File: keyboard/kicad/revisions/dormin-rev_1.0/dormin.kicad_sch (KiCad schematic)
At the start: 59 parts, among them J2 Conn_01x07_Socket, SW1 SW_Push, SW10 SW_Push, SW11 SW_Push, SW12 SW_Push, SW13 SW_Push, SW14 SW_Push, SW15 SW_Push, SW16 SW_Push, SW17 SW_Push, SW18 SW_Push, SW19 SW_Push, SW2 SW_Push, SW20 SW_Push, SW3 SW_Push, SW4 SW_Push, SW5 SW_Push, SW6 SW_Push, SW7 SW_Push, SW8 SW_Push, SW9 SW_Push, U2 ER_OLEDM0.91_1x-I2C, U3 XIAO-nRF52840-Plus-SMD

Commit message: feat: update schematics
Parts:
- added D27: D_Schottky, symbol Device:D_Schottky
- added D28: SMF5V0A, Diode_SMD:D_SMF, symbol Diode:SMF5V0A
- added F2: Polyfuse, symbol Device:Polyfuse
- added J3: Pogo Connector, symbol Connector:Conn_01x04_Pin
- added R5, R6: 33R, symbol Device:R
- added U4: TPD2E2U06DCK, Package_TO_SOT_SMD:SOT-323_SC-70, symbol Power_Protection:TPD2E2U06DCK
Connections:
- net BAT- is gone; now on net GND: U3.29 (GND)
- net +3V3: no longer D21.3 (VDD), D22.3 (VDD), D23.3 (VDD), D24.3 (VDD), J2.4 (Pin_4), U3.12 (3V3_OUT)
- net D18: no longer U3.22 (D18_MISO)
- net D8: no longer U3.9 (D8_SCK)
- net D9: no longer U3.10 (D9_MISO)
- net GND: now also JST1.1 (Pin_1), D28.1 (A1), J3.1 (Pin_1), U4.3; no longer JST1.2 (Pin_2)
- net MOSI: no longer U3.23 (D19_MOSI)
- net SCK: no longer U3.21 (D17_SCK)
- net at BT1.1 (+), PSW1.3 (C): now also JST1.2 (Pin_2); no longer JST1.1 (Pin_1)
- net USB_VBUS: now reaches U3.14 (VBUS)
- net USB_VBUS: now also F2.1
- net LED renamed COL4
- net COL4: now also SW13.2, SW19.2, SW2.2, SW7.2; no longer D21.2 (DIN)
- net col0 renamed COL0
- net col1 renamed COL1
- net COL1: now also U3.8 (D7_RX); no longer U3.15 (D11_SD)
- net col2 renamed COL2
- net COL2: now also U3.9 (D8_SCK); no longer U3.16 (D12_SCK)
- net col3 renamed COL3
- net COL3: now also U3.10 (D9_MISO); no longer U3.17 (D13_WS)
- removed net col4: SW13.2, SW19.2, SW2.2, SW7.2, U3.18 (D14_NFC1)
- net col5 renamed COL5
- net COL5: now also U3.15 (D11_SD); no longer U3.8 (D7_RX)
- net row0 renamed ROW0
- net row1 renamed ROW1
- net row2 renamed ROW2
- net row3 renamed ROW3
- new net: J3.3 (Pin_3), R5.1, U4.1
- new net: D27.1 (K), D28.2 (A2), J3.2 (Pin_2)
- new net: J3.4 (Pin_4), R6.2, U4.2
- new net: D27.2 (A), F2.2
- new net EXT_D17: R6.1, U3.21 (D17_SCK)
- new net EXT_D19: R5.2, U3.23 (D19_MOSI)
- new net RGB_DATA: D21.2 (DIN), U3.17 (D13_WS)
- new net VCC: D21.3 (VDD), D22.3 (VDD), D23.3 (VDD), D24.3 (VDD), J2.4 (Pin_4), U3.12 (3V3_OUT)
- no-connect marks 3 -> 5
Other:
- note added: "Pogo Extension"
- moved on the sheet: BT1, JST1, MH1, MH2, MH3, MH4, PSW1, TP1, TP2, U3

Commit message: feat: clean pcb and outline
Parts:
- removed D25: 1N4148W, Diode_SMD:D_SOD-123, symbol Diode:1N4148W
- removed RES1: RotaryEncoder_Switch, willkeebs_peripherals:RotaryEncoder_Alps_EC11E-Switch_Vertical_H20mm-keebio_modified, symbol Device:RotaryEncoder_Switch
- removed U2: ER_OLEDM0.91_1x-I2C, Display:ER_OLEDM0.91_1x-I2C, symbol Display_Graphic:ER_OLEDM0.91_1x-I2C
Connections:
- net D18 is gone; now on net EXTD: J2.7 (Pin_7)
- net D8 is gone; now on net EXTA: J2.1 (Pin_1)
- net D9 is gone; now on net EXTB: J2.6 (Pin_6)
- net MOSI is gone; now on net GND: J2.2 (Pin_2)
- net SCK is gone; now on net VCC: J2.3 (Pin_3)
- net GND: no longer J2.5 (Pin_5)
- net SCL: now also J2.4 (Pin_4)
- net SDA: now also J2.5 (Pin_5)
- net VCC: no longer J2.4 (Pin_4)
- net EXTA: now reaches U3.16 (D12_SCK)
- net EXTB: now reaches U3.18 (D14_NFC1)
- net EXTD: now reaches U3.22 (D18_MISO)
- net ENCA renamed EXTG
- net ENCB renamed EXTF
- net EXT_D17 renamed EXTE
- net EXT_D19 renamed EXTC
- no-connect marks 5 -> 2
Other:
- note removed: "OLED SSD1306"
- moved on the sheet: BT1, J2, JST1, PSW1, TP1, TP2, U3

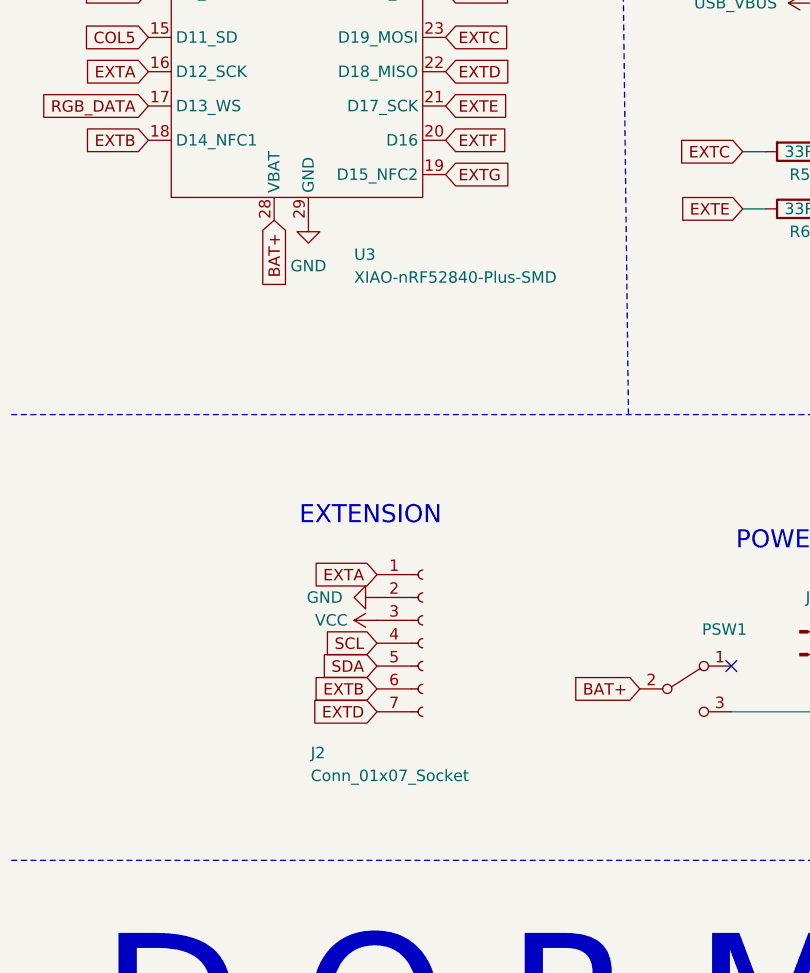
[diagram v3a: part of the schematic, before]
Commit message: feat: start PCB placement
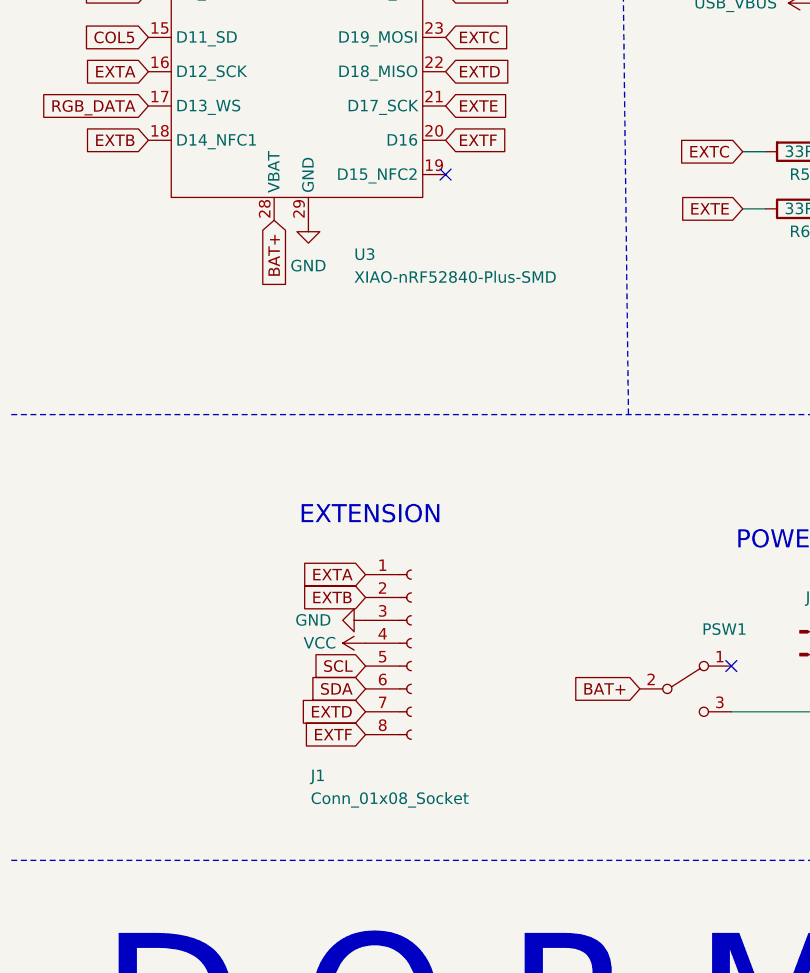
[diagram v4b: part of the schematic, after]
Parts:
- removed J2: Conn_01x07_Socket, symbol Connector:Conn_01x07_Socket
- added J1: Conn_01x08_Socket, Connector_PinSocket_2.54mm:PinSocket_1x08_P2.54mm_Vertical, symbol Connector:Conn_01x08_Socket
- J3: footprint (none) -> Connector_PinSocket_2.54mm:PinSocket_1x04_P2.54mm_Vertical_SMD_Pin1Left
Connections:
- net EXTA: now also J1.1 (Pin_1)
- net EXTB: now also J1.2 (Pin_2)
- net EXTD: now also J1.7 (Pin_7)
- net EXTF: now also J1.8 (Pin_8)
- net GND: now also J1.3 (Pin_3)
- net SCL: now also J1.5 (Pin_5)
- net SDA: now also J1.6 (Pin_6)
- net VCC: now also J1.4 (Pin_4)
- net EXTG: no longer names the net of U3.19 (D15_NFC2)
- no-connect marks 2 -> 3

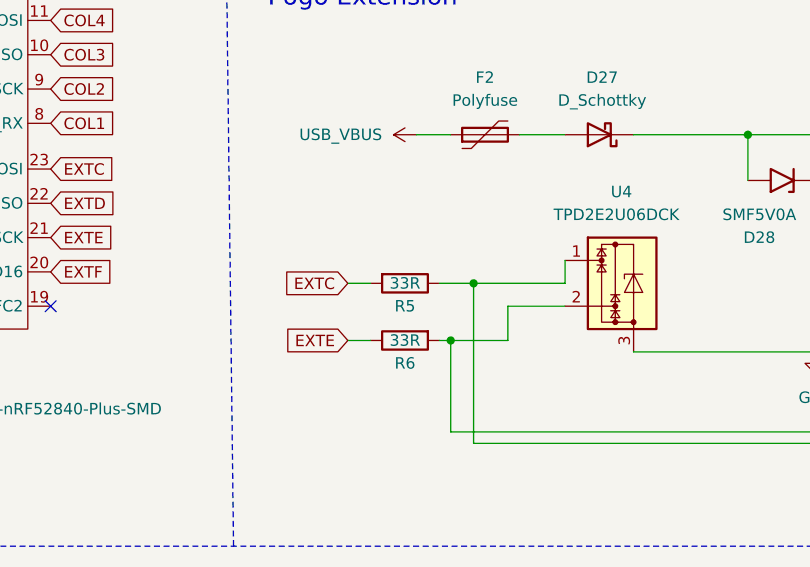
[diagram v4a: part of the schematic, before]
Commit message: feat: added pogo-pin pcb components
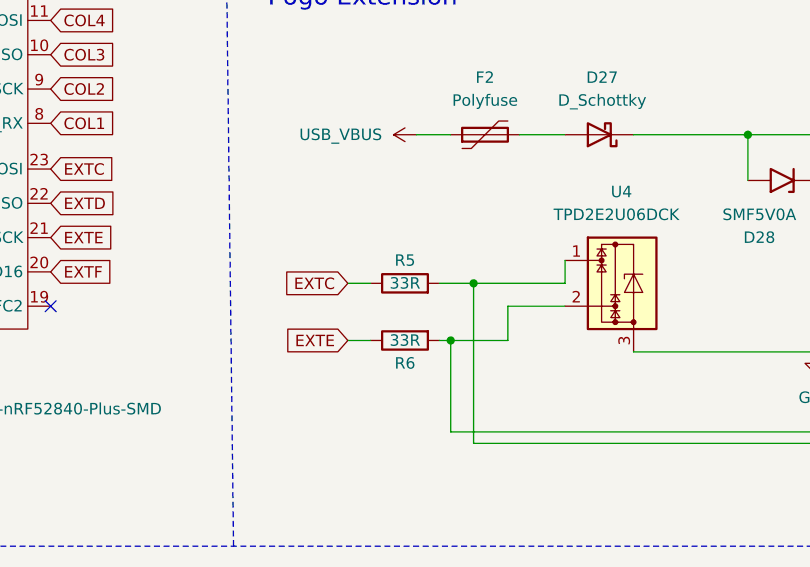
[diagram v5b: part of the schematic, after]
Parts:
- D27: footprint (none) -> Diode_SMD:Nexperia_CFP3_SOD-123W
- F2: footprint (none) -> Fuse:Fuse_1206_3216Metric
- R5, R6: footprint (none) -> Resistor_SMD:R_0402_1005Metric
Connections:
- net EXTC: now also R5.1; no longer R5.2
- net at J3.3 (Pin_3), U4.1: now also R5.2; no longer R5.1
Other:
- moved on the sheet: R5
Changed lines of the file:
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@@
 	(symbol
 		(lib_id "Device:R")
-		(at 100.33 87.63 270)
+		(at 100.33 87.63 90)
 		(unit 1)
 		(body_style 1)
@@
 		(dnp no)
 		(property "Reference" "R5"
-			(at 100.33 90.17 90)
+			(at 100.33 85.09 90)
 			(show_name no)
 			(do_not_autoplace no)
@@
 			)
 		)
-		(property "Footprint" ""
-			(at 100.33 85.852 90)
+		(property "Footprint" "Resistor_SMD:R_0402_1005Metric"
+			(at 100.33 89.408 90)
 			(hide yes)
 			(show_name no)
@@
 			)
 		)
-		(property "Footprint" ""
+		(property "Footprint" "Diode_SMD:Nexperia_CFP3_SOD-123W"
 			(at 121.92 71.12 0)
 			(hide yes)
@@
 			)
 		)
-		(property "Footprint" ""
+		(property "Footprint" "Resistor_SMD:R_0402_1005Metric"
 			(at 100.33 92.202 90)
 			(hide yes)
@@
 			)
 		)
-		(property "Footprint" ""
+		(property "Footprint" "Fuse:Fuse_1206_3216Metric"
 			(at 114.3 69.85 0)
 			(hide yes)

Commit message: feat: added support for white backlight (wip)
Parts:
- added C1: 100nF, Capacitor_SMD:C_0603_1608Metric, symbol Device:C
- added C2: 10uF, Capacitor_SMD:C_0603_1608Metric, symbol Device:C
- added D25, D26, D29, D30, D31, D32, D33, D34, D35, D36, D37, D38, D39, D40, D41, D42, D43, D44, D45, D46: LED, willkeebs_components:LED_MHT151WDT, symbol Device:LED
- added Q1: HX2302A, Package_TO_SOT_SMD:SOT-23, symbol Transistor_FET:AO3400A
- added R1, R10, R11, R12, R13, R14, R15, R16, R17, R18, R19, R2, R20, R21, R22, R3, R4, R7, R8, R9: 1K, Resistor_SMD:R_0603_1608Metric, symbol Device:R
- added R706: 100R, Resistor_SMD:R_0603_1608Metric, symbol Device:R
- added R707: 10k, Resistor_SMD:R_0603_1608Metric, symbol Device:R
- added TP3: TestPoint, symbol Connector:TestPoint
- SW1, SW10, SW11, SW12, SW13, SW14, SW15, SW16, SW17, SW18, SW19, SW2, SW20, SW3, SW4, SW5, SW6, SW7, SW8, SW9: footprint willkeebs_keyboard:SW_MX_Choc_Hotswap -> willkeebs_keyboard:NF_LED_1206_SW_KS33_3_0_HS_1U
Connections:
- net GND: now also JST1.2 (Pin_2), C1.2, C2.2, Q1.2 (S), R707.1; no longer JST1.1 (Pin_1)
- net LED_PWM: now reaches U3.19 (D15_NFC2)
- net LED_PWM: now also R706.1
- net BAT+: no longer names the net of PSW1.2 (B)
- net BAT+: now also BT1.1 (+), JST1.1 (Pin_1); no longer U3.28 (VBAT)
- net USB_VBUS renamed 5V
- net VCC renamed 3V3
- new net: D40.1 (K), R16.1
- new net: D45.1 (K), R21.1
- new net: D46.1 (K), R22.1
- new net: D37.1 (K), R13.1
- new net: D29.1 (K), R3.1
- new net: Q1.1 (G), R706.2, R707.2
- new net: D34.1 (K), R10.1
- new net: D25.1 (K), R1.1
- new net: D31.1 (K), R7.1
- new net: D39.1 (K), R15.1
- new net: D38.1 (K), R14.1
- new net: D43.1 (K), R19.1
- new net: D41.1 (K), R17.1
- new net: D42.1 (K), R18.1
- new net: D44.1 (K), R20.1
- new net: D35.1 (K), R11.1
- new net: D32.1 (K), R8.1
- new net: D33.1 (K), R9.1
- new net: D26.1 (K), R2.1
- new net: D30.1 (K), R4.1
- new net: D36.1 (K), R12.1
- new net LED_SWITCH: Q1.3 (D), R1.2, R10.2, R11.2, R12.2, R13.2, R14.2, R15.2, R16.2, R17.2, R18.2, R19.2, R2.2, R20.2, R21.2, R22.2, R3.2, R4.2, R7.2, R8.2, R9.2
- new net LED_VCC: C1.1, C2.1, D25.2 (A), D26.2 (A), D29.2 (A), D30.2 (A), D31.2 (A), D32.2 (A), D33.2 (A), D34.2 (A), D35.2 (A), D36.2 (A), D37.2 (A), D38.2 (A), D39.2 (A), D40.2 (A), D41.2 (A), D42.2 (A), D43.2 (A), D44.2 (A), D45.2 (A), D46.2 (A), PSW1.3 (C), TP3.1, U3.28 (VBAT)
- no-connect marks 3 -> 2
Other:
- note added: "BACKLIGHT LEDS"
- note added: "LED PWM MOSFET"
- moved on the sheet: BT1, JST1, PSW1, TP1, TP2, U3

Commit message: feat: organize schematics sheet
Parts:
- removed J1: Conn_01x08_Socket, Connector_PinSocket_2.54mm:PinSocket_1x08_P2.54mm_Vertical, symbol Connector:Conn_01x08_Socket
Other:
- note added: "Status LEDs"
- note removed: "EXTENSION"
- note removed: "LEDs SK6812MINI-E"
- moved on the sheet: BT1, C1, C2, D1, D10, D11, D12, D13, D14, D15, D16, D17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

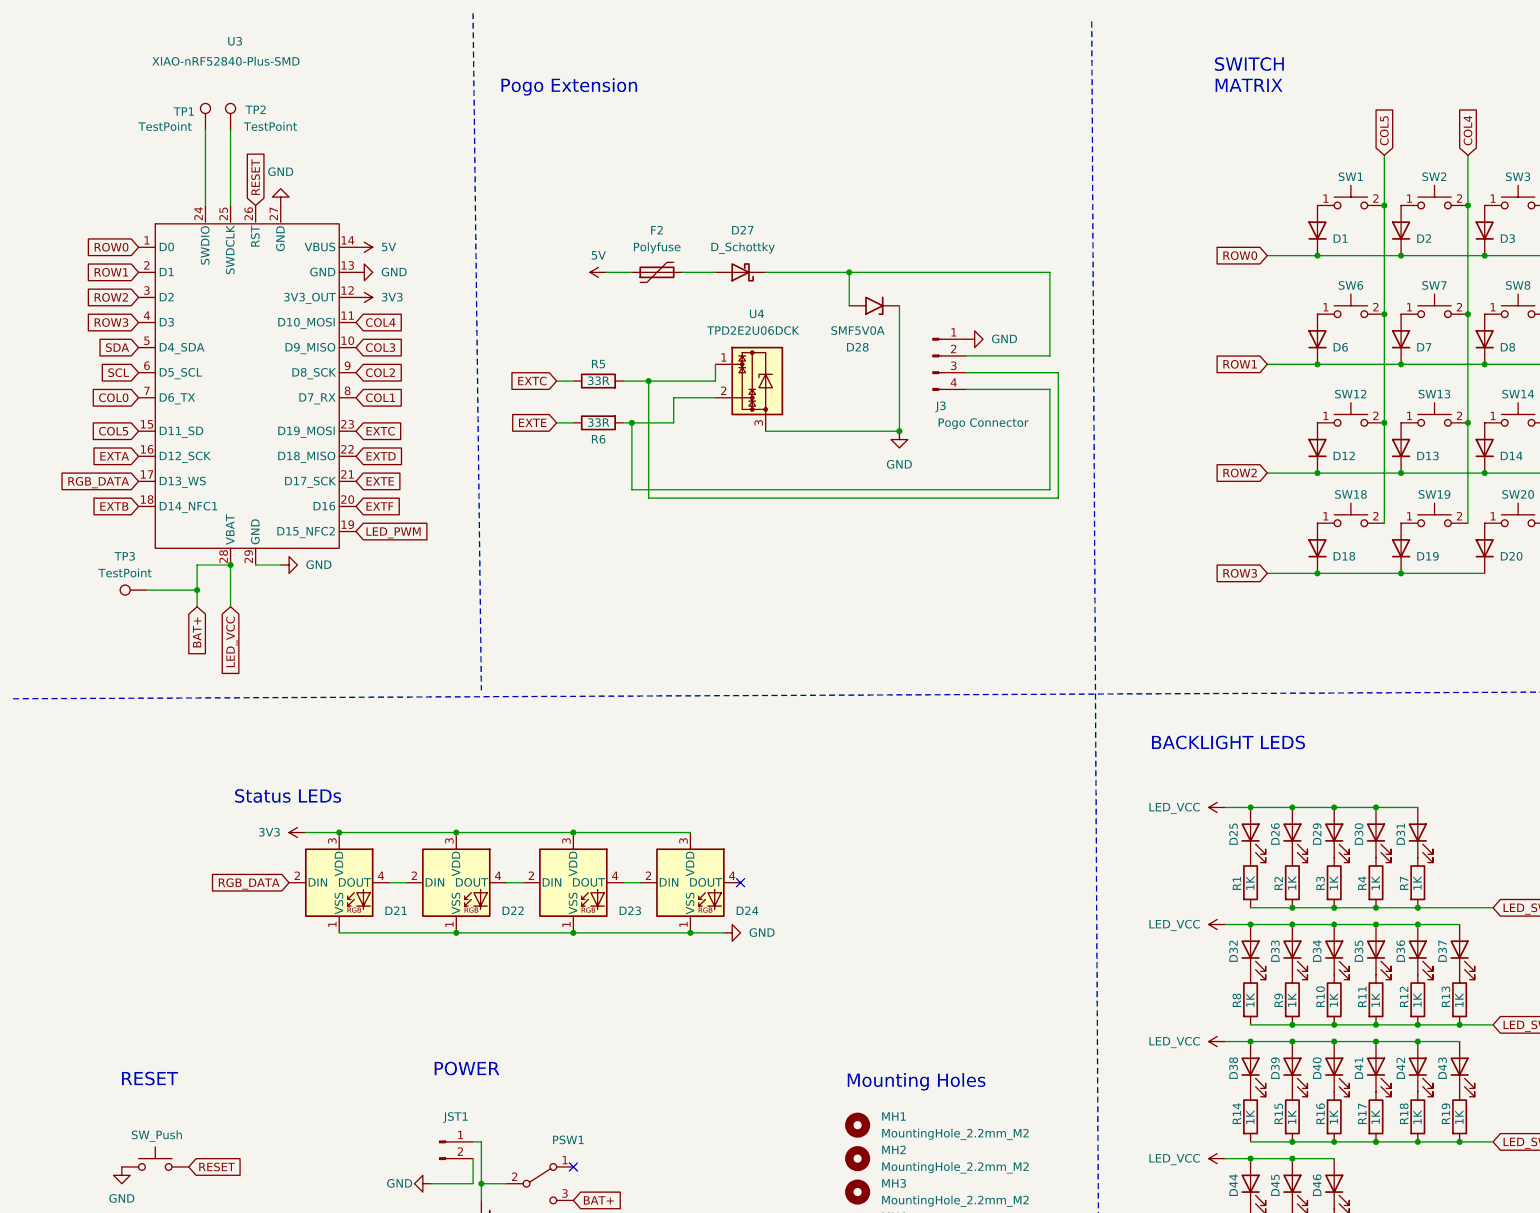
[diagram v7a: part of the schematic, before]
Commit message: feat: added 4-pin extension support
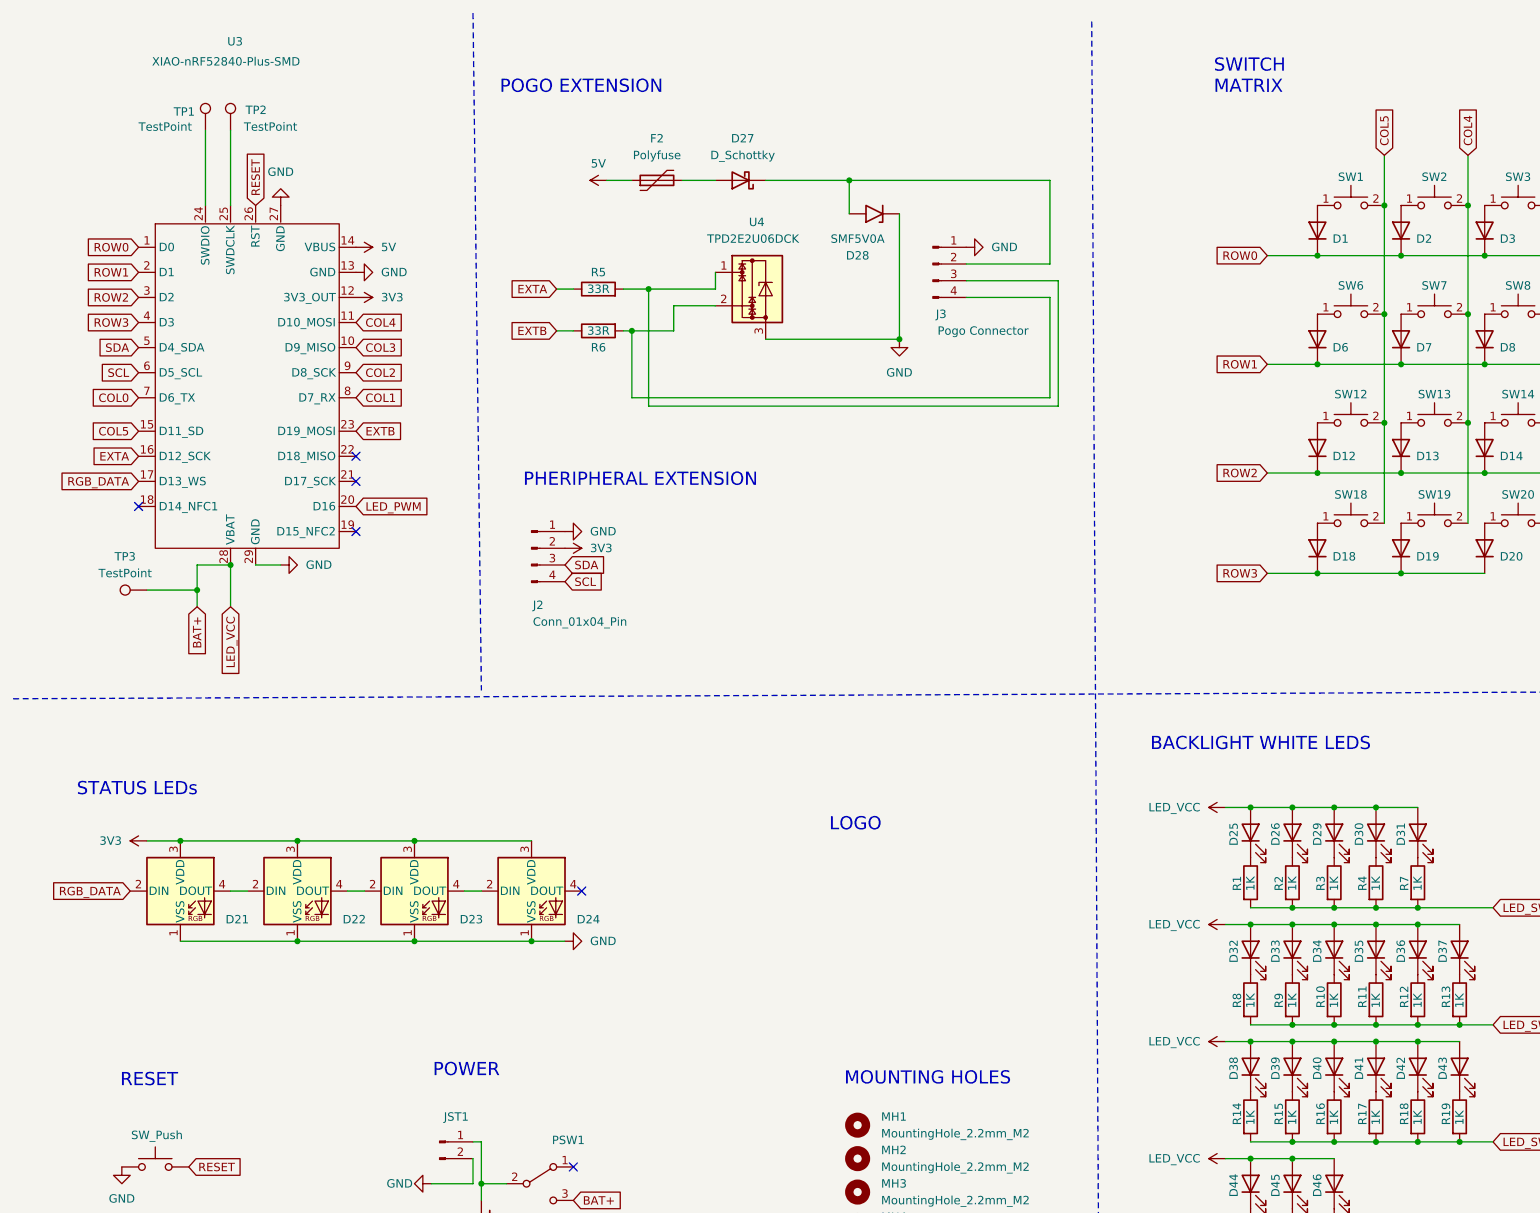
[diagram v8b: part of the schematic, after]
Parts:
- added J2: Conn_01x04_Pin, symbol Connector:Conn_01x04_Pin
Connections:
- net EXTF is gone; now on net LED_PWM: U3.20 (D16)
- net 3V3: now also J2.2 (Pin_2)
- net EXTA: now also R5.1
- net EXTB: now also R6.1, U3.23 (D19_MOSI); no longer U3.18 (D14_NFC1)
- net GND: now also J2.1 (Pin_1)
- net LED_PWM: no longer U3.19 (D15_NFC2)
- net SCL: now also J2.4 (Pin_4)
- net SDA: now also J2.3 (Pin_3)
- removed net EXTC: R5.1, U3.23 (D19_MOSI)
- net EXTD: no longer names the net of U3.22 (D18_MISO)
- net EXTE: no longer names the net of U3.21 (D17_SCK)
- net EXTE: no longer R6.1
- no-connect marks 2 -> 6
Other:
- note added: "BACKLIGHT WHITE LEDS"
- note added: "LOGO"
- note added: "MOUNTING HOLES"
- note added: "PHERIPHERAL EXTENSION"
- note added: "POGO EXTENSION"
- note added: "STATUS LEDs"
- note removed: "BACKLIGHT LEDS"
- note removed: "Mounting Holes"
- note removed: "Pogo Extension"
- note removed: "Status LEDs"
- moved on the sheet: D21, D22, D23, D24, D27, D28, F2, J3, R5, R6, U4
